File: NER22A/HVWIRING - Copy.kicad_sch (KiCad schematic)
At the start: 7 parts

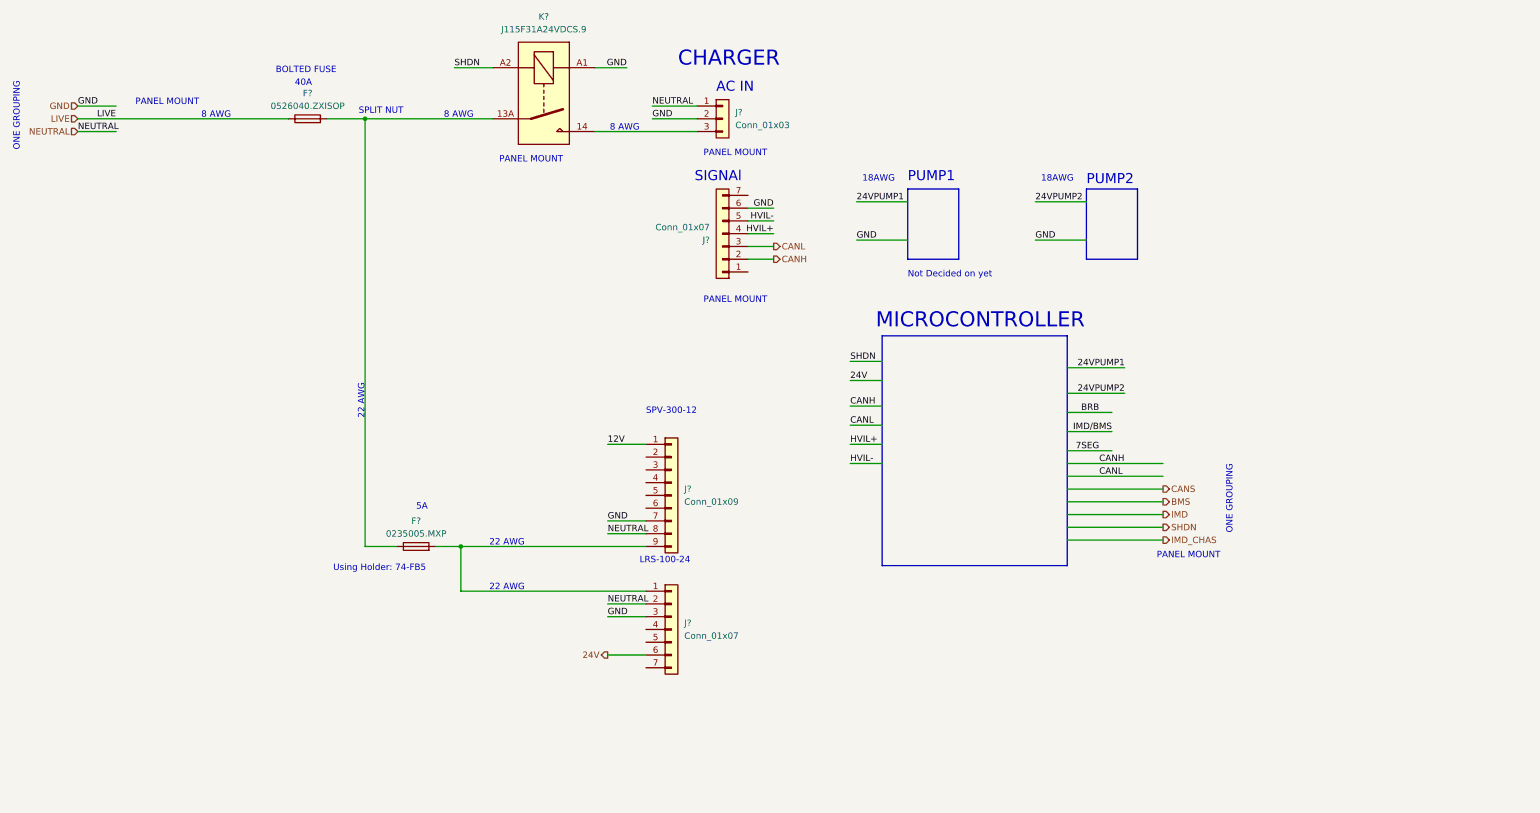
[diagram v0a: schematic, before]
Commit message: Finished wiring diagram
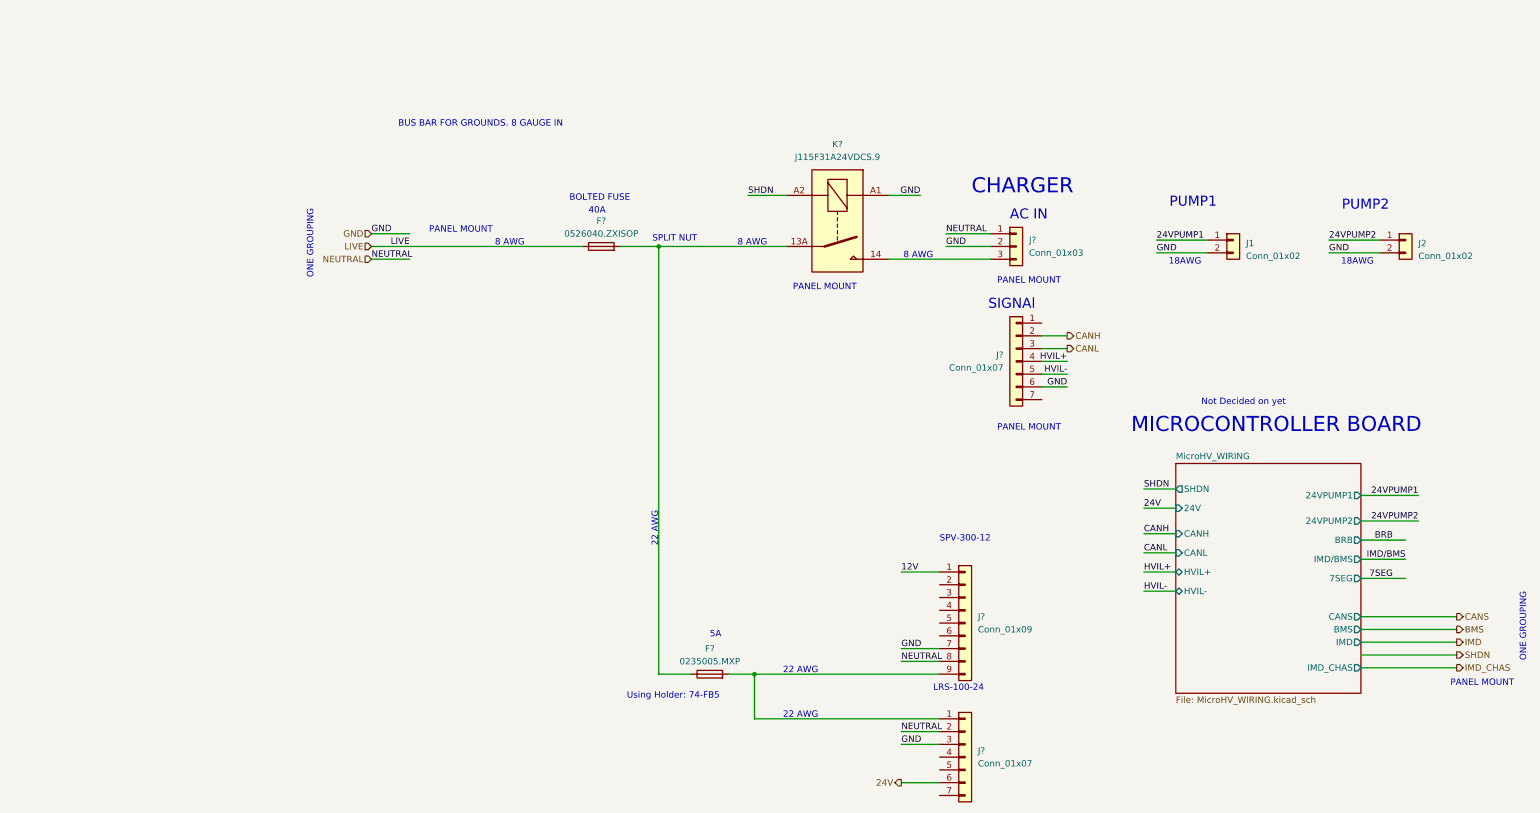
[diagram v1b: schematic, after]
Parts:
- added J1, J2: Conn_01x02, symbol Connector_Generic:Conn_01x02
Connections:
- net 24VPUMP1: now also J1.1 (Pin_1)
- net 24VPUMP2: now also J2.1 (Pin_1)
- net GND: now also J1.2 (Pin_2), J2.2 (Pin_2)
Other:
- added sheet MicroHV_WIRING (MicroHV_WIRING.kicad_sch)
- note added: "BUS BAR FOR GROUNDS. 8 GAUGE IN"
- note added: "MICROCONTROLLER BOARD"
- note removed: "MICROCONTROLLER"
- moved on the sheet: F?, J?, K?
